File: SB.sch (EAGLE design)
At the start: 48 parts, among them IC1 ATMEGA32U4NT-TQFP, IC2 HX711-SOP16L, J2 RJ12, J3 AUDIO-JACK-PJ321, J5 USB-C-16P-16P, K1 HE721C-DIP, Q1 2N7002, Q2 2N7002, Q3 2N3906, SW1 SWITCH-SPDT-4TABSSMT

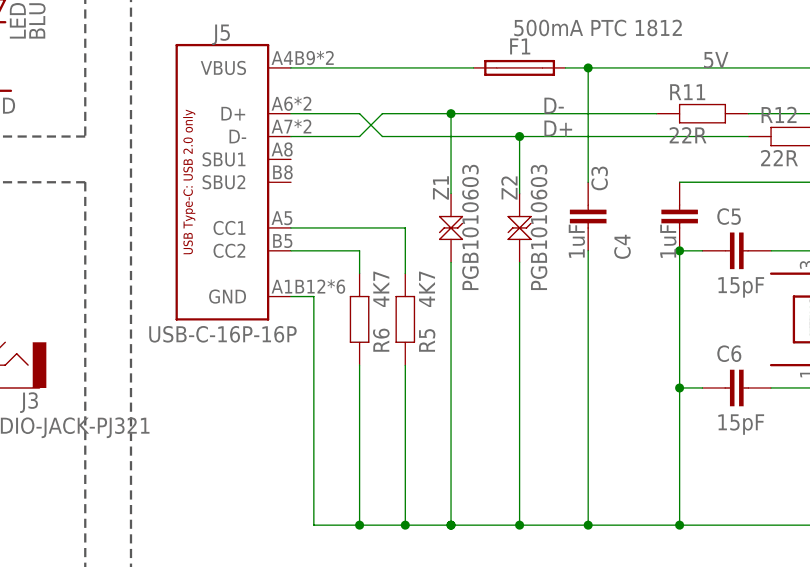
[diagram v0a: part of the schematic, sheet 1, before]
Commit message: Synch with Fusion 360
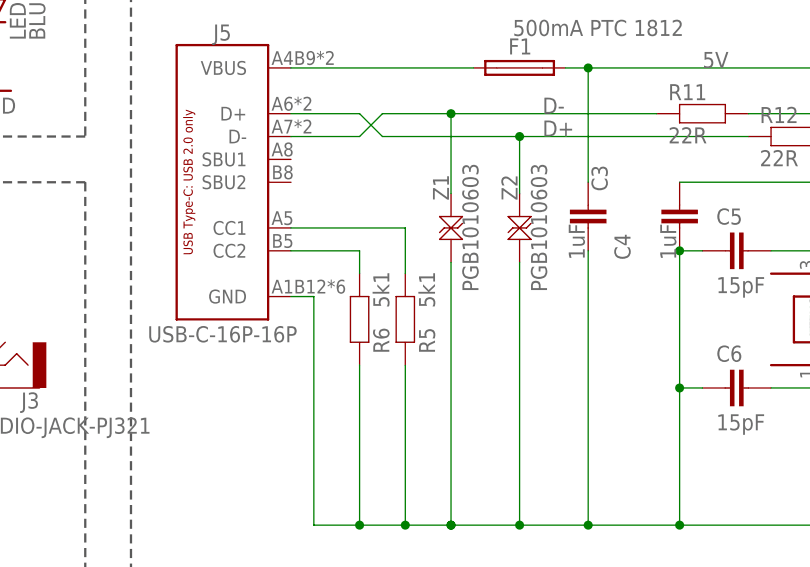
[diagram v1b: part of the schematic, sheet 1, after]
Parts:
- R5, R6: value 4K7 -> 5k1
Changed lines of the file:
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@@
 <part name="IC2" library="SuperHouse-ICs" library_urn="urn:adsk.eagle:library:11768868" deviceset="HX711" device="-SOP16L" package3d_urn="urn:adsk.eagle:package:17215012/2"/>
 <part name="J5" library="SuperHouse-Connectors" library_urn="urn:adsk.eagle:library:11765989" deviceset="USB-C-16P" device="-16P" package3d_urn="urn:adsk.eagle:package:17045956/2"/>
-<part name="R5" library="SuperHouse-DiscreteSemi" library_urn="urn:adsk.eagle:library:11768461" deviceset="RESISTOR" device="0603" package3d_urn="urn:adsk.eagle:package:11768543/2" value="4K7"/>
-<part name="R6" library="SuperHouse-DiscreteSemi" library_urn="urn:adsk.eagle:library:11768461" deviceset="RESISTOR" device="0603" package3d_urn="urn:adsk.eagle:package:11768543/2" value="4K7"/>
+<part name="R5" library="SuperHouse-DiscreteSemi" library_urn="urn:adsk.eagle:library:11768461" deviceset="RESISTOR" device="0603" package3d_urn="urn:adsk.eagle:package:11768543/2" value="5k1"/>
+<part name="R6" library="SuperHouse-DiscreteSemi" library_urn="urn:adsk.eagle:library:11768461" deviceset="RESISTOR" device="0603" package3d_urn="urn:adsk.eagle:package:11768543/2" value="5k1"/>
 <part name="C8" library="SuperHouse-DiscreteSemi" library_urn="urn:adsk.eagle:library:11768461" deviceset="CAP" device="0603" package3d_urn="urn:adsk.eagle:package:7066315/6" value="100nF"/>
 <part name="C9" library="SuperHouse-DiscreteSemi" library_urn="urn:adsk.eagle:library:11768461" deviceset="CAP" device="0603" package3d_urn="urn:adsk.eagle:package:7066315/6" value="100nF"/>
@@
 <part name="C11" library="SuperHouse-DiscreteSemi" library_urn="urn:adsk.eagle:library:11768461" deviceset="CAP" device="0603" package3d_urn="urn:adsk.eagle:package:7066315/6" value="100nF"/>
 <part name="C12" library="SuperHouse-DiscreteSemi" library_urn="urn:adsk.eagle:library:11768461" deviceset="CAP" device="0603" package3d_urn="urn:adsk.eagle:package:7066315/6" value="10uF"/>
-<part name="SW1" library="SuperHouse-Switches" library_urn="urn:adsk.eagle:library:11744182" deviceset="SWITCH-SPDT-4TABS" device="SMT" package3d_urn="urn:adsk.eagle:package:7066359/1"/>
+<part name="SW1" library="SuperHouse-Switches" library_urn="urn:adsk.eagle:library:11744182" deviceset="SWITCH-SPDT-4TABS" device="SMT" package3d_urn="urn:adsk.eagle:package:7066359/2"/>
 <part name="GND10" library="SuperHouse-SupplySymbols" library_urn="urn:adsk.eagle:library:11790503" deviceset="GND" device=""/>
 </parts>

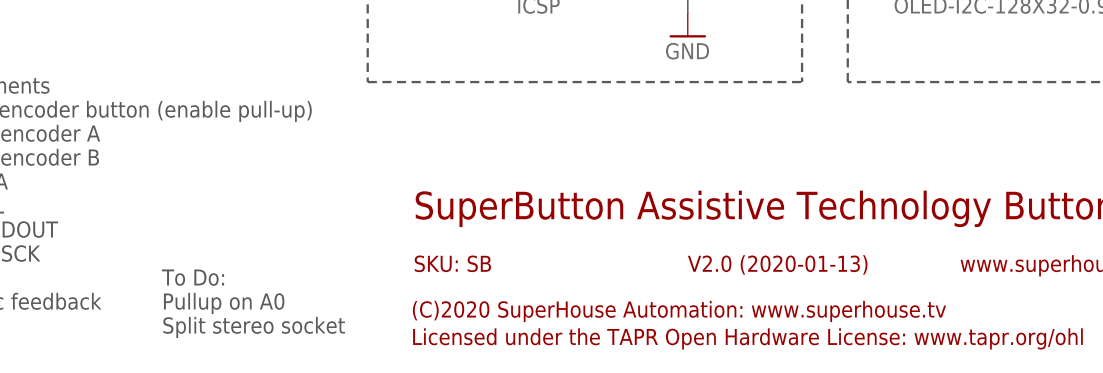
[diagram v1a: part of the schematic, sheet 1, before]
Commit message: Added mounting holes for v2.1 release
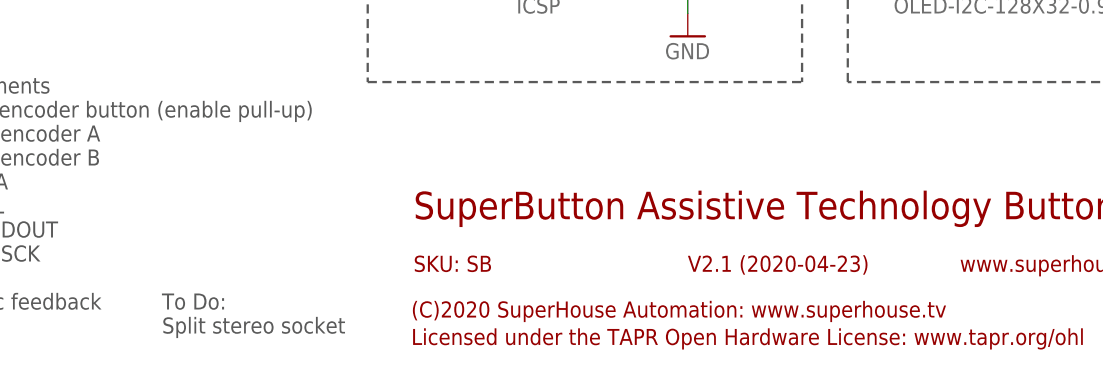
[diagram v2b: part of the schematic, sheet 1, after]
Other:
- note added: "To Do: Split stereo socket"
- note added: "V2.1 (2020-04-23)"
- note removed: "To Do: Pullup on A0 Split stereo socket"
- note removed: "V2.0 (2020-01-13)"
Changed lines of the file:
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@@
 <?xml version="1.0" encoding="utf-8"?>
 <!DOCTYPE eagle SYSTEM "eagle.dtd">
-<eagle version="9.5.2">
+<eagle version="9.6.1">
 <drawing>
 <settings>
@@
 <text x="86.36" y="170.18" size="2.54" layer="94" ratio="12">ATmega32u4 MCU</text>
 <text x="142.24" y="20.32" size="3.048" layer="94">SuperButton Assistive Technology Button</text>
-<text x="172.72" y="14.478" size="1.778" layer="94">V2.0 (2020-01-13)</text>
+<text x="172.72" y="14.478" size="1.778" layer="94">V2.1 (2020-04-23)</text>
 <text x="142.24" y="14.478" size="1.778" layer="94">SKU: SB</text>
 <text x="141.986" y="9.398" size="1.778" layer="94">(C)2020 SuperHouse Automation: www.superhouse.tv</text>
@@
 <text x="39.37" y="102.235" size="1.27" layer="97">NC</text>
 <text x="114.3" y="7.62" size="1.778" layer="97">To Do:
-Pullup on A0
 Split stereo socket</text>
 </plain>
